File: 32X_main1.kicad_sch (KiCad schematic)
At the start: 27 parts, among them IC504 315-5818, IC505 315-5805, IC509 74AC04

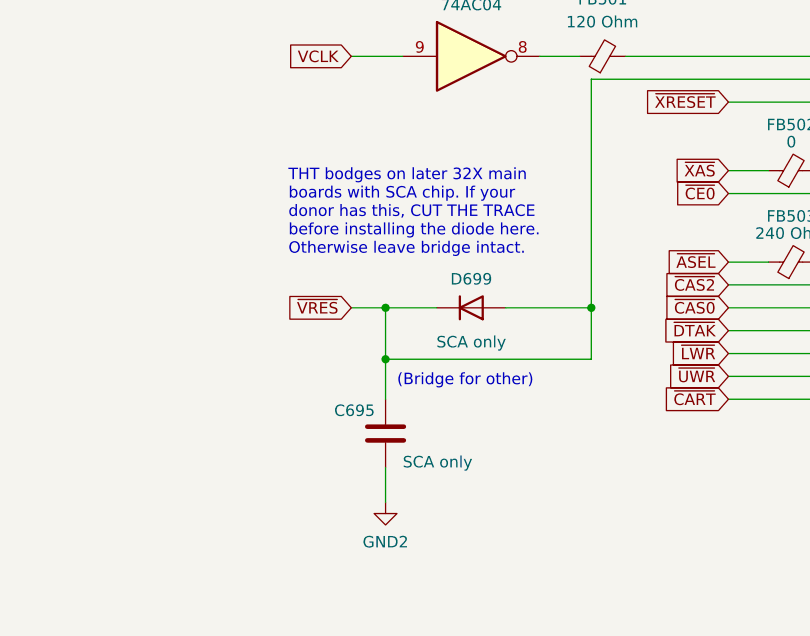
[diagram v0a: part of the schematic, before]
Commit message: Update documentation about D699, rename C695 to C553 to indicate origin (issue #7).
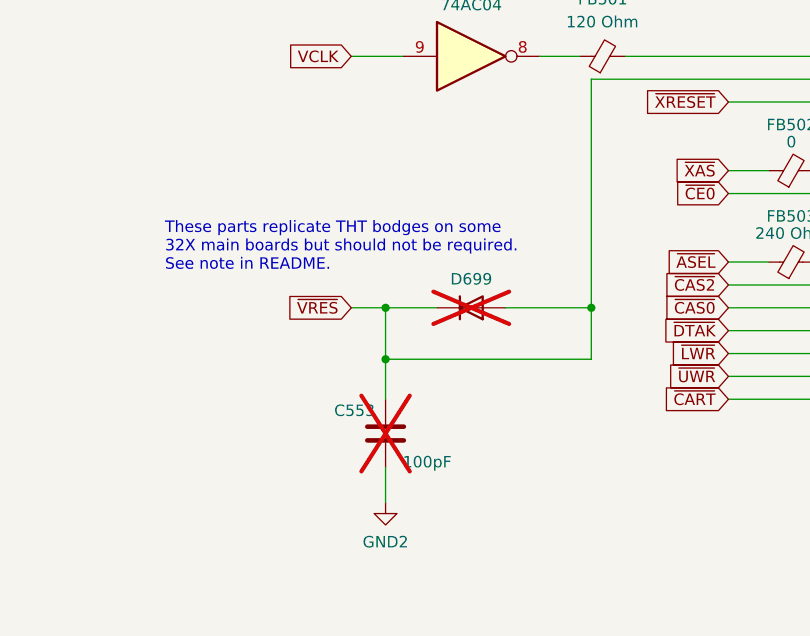
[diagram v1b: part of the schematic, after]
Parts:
- C553: renamed from C695; value SCA only -> 100pF; now not fitted; now left out of the parts list
- D699: value SCA only -> (none); now not fitted; now left out of the parts list
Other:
- note added: "These parts replicate THT bodges on some 32X main boards but should not be required. See note in README."
- note removed: "(Bridge for other)"
- note removed: "THT bodges on later 32X main boards with SCA chip. If your donor has this, CUT THE TRACE before installing the diode here. Otherwise leave bridge intact."
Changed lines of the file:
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@@
 		)
 	)
-	(text "(Bridge for other)"
-		(exclude_from_sim no)
-		(at 109.855 193.675 0)
-		(effects
-			(font
-				(size 1.27 1.27)
-			)
-			(justify left bottom)
-		)
-	)
 	(text "VA1 ONLY"
 		(exclude_from_sim no)
@@
 		)
 	)
-	(text "THT bodges on later 32X main\nboards with SCA chip. If your\ndonor has this, CUT THE TRACE\nbefore installing the diode here.\nOtherwise leave bridge intact."
+	(text "These parts replicate THT bodges on some\n32X main boards but should not be required.\nSee note in README.\n"
 		(exclude_from_sim no)
-		(at 97.79 179.07 0)
+		(at 84.074 180.848 0)
 		(effects
 			(font
@@
 		(unit 1)
 		(exclude_from_sim no)
-		(in_bom yes)
+		(in_bom no)
 		(on_board yes)
-		(dnp no)
-		(property "Reference" "C695"
+		(dnp yes)
+		(property "Reference" "C553"
 			(at 102.87 196.215 0)
 			(effects
@@
 			)
 		)
-		(property "Value" "SCA only"
+		(property "Value" "100pF"
 			(at 110.49 201.93 0)
 			(effects
@@
 			(project "Neptune"
 				(path "/bcc23b51-b742-4ae5-9dd6-d96a24058944/a9caee2e-423b-443e-a11f-5841882e2685"
-					(reference "C695")
+					(reference "C553")
 					(unit 1)
 				)
@@
 		(unit 1)
 		(exclude_from_sim no)
-		(in_bom yes)
+		(in_bom no)
 		(on_board yes)
-		(dnp no)
+		(dnp yes)
 		(property "Reference" "D699"
 			(at 118.11 181.61 0)
@@
 			)
 		)
-		(property "Value" "SCA only"
+		(property "Value" ""
 			(at 118.11 188.595 0)
 			(effects

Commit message: Tie SH2 NMI pins to VCC as per original 32X main board (not obvious from schematic).
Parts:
- D699: value (none) -> ~
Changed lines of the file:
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@@
 			)
 		)
-		(property "Value" ""
+		(property "Value" "~"
 			(at 118.11 188.595 0)
 			(effects
